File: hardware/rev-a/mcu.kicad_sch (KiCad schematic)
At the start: 46 parts, among them J10 Conn_01x05, J11 Conn_01x04, J12 Conn_01x05, J13 Conn_01x04, J14 Conn_01x04, J15 Conn_01x04, J16 Conn_01x02, Q1 NPN, SW1 SW_Push, U3 MDBT42Q-512K, U4 DS3231MZ, U5 DRV2605LDGS

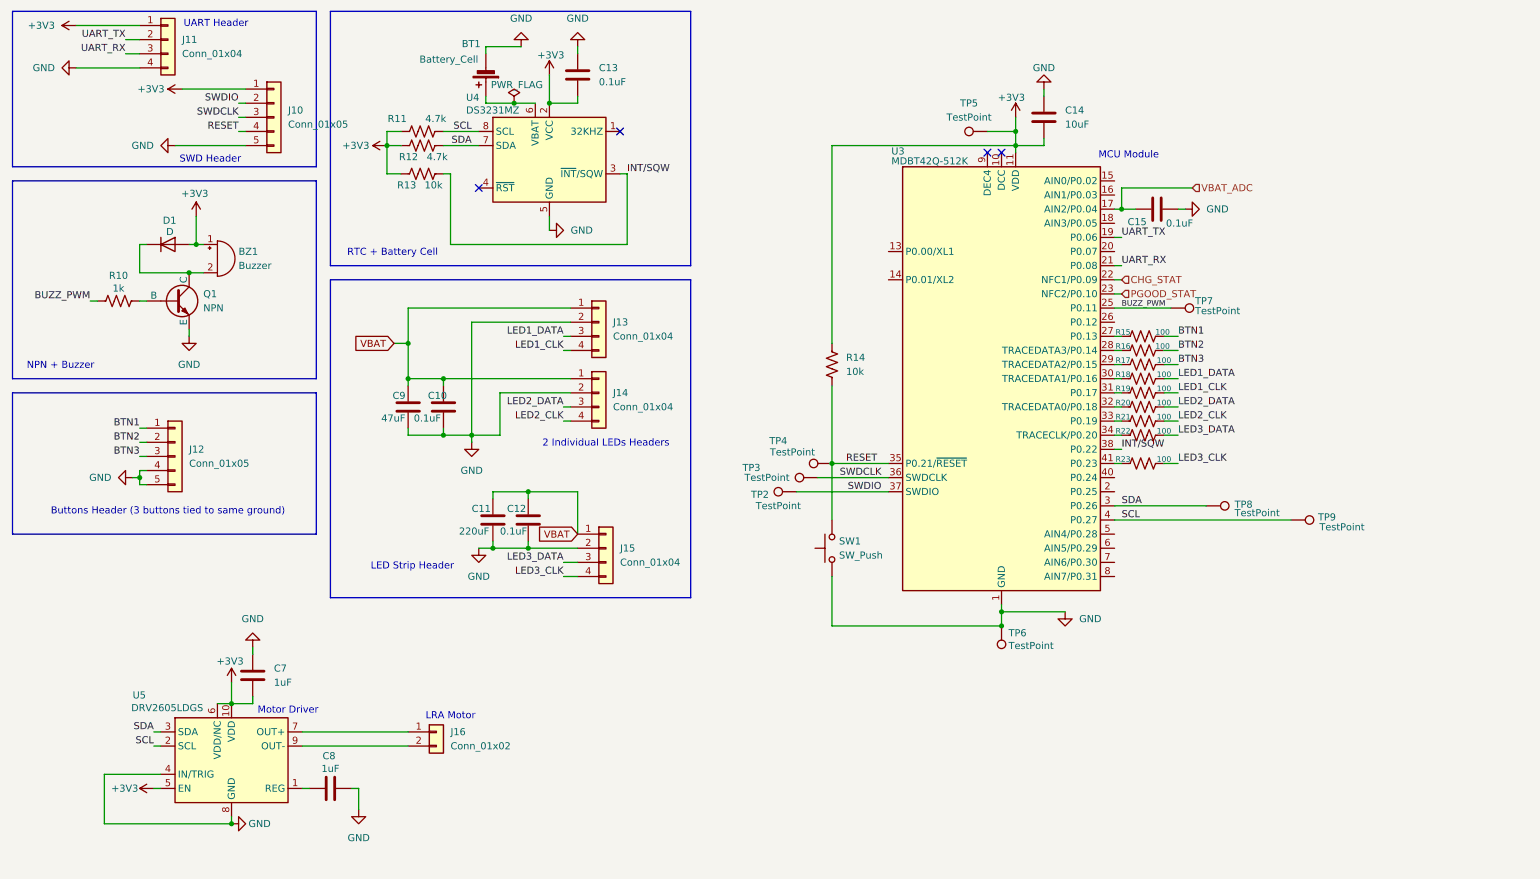
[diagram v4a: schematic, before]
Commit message: Assign footprints and add additional bypass caps
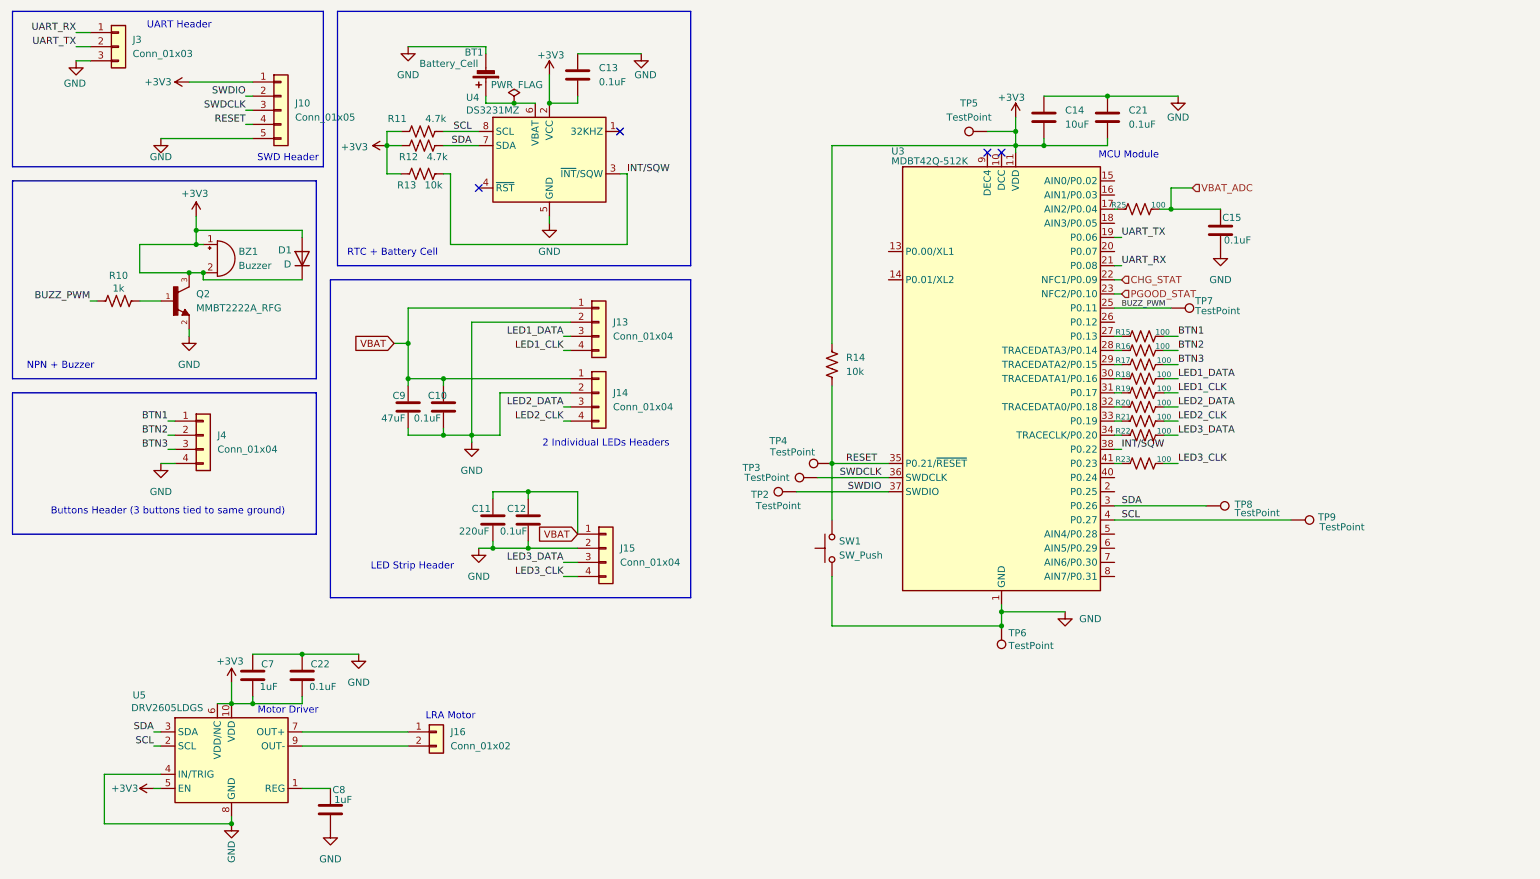
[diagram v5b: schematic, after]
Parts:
- removed J11: Conn_01x04, Connector_PinHeader_2.54mm:PinHeader_1x04_P2.54mm_Vertical, symbol Connector_Generic:Conn_01x04
- removed J12: Conn_01x05, Connector_JST:JST_PH_B5B-PH-K_1x05_P2.00mm_Vertical, symbol Connector_Generic:Conn_01x05
- removed Q1: NPN, Package_TO_SOT_SMD:SOT-23, symbol Simulation_SPICE:NPN
- added C21, C22: 0.1uF, Capacitor_SMD:C_0603_1608Metric, symbol Device:C
- added J3: Conn_01x03, Connector_PinHeader_2.54mm:PinHeader_1x03_P2.54mm_Vertical, symbol Connector_Generic:Conn_01x03
- added J4: Conn_01x04, Connector_PinHeader_2.54mm:PinHeader_1x04_P2.54mm_Vertical, symbol Connector_Generic:Conn_01x04
- added Q2: MMBT2222A_RFG, Package_TO_SOT_SMD:SOT-23, symbol MMBT2222A_RFG:MMBT2222A_RFG
- added R25: 100, Resistor_SMD:R_0603_1608Metric, symbol Device:R_US
- BT1: footprint Battery:BatteryHolder_Keystone_103_1x20mm -> Battery:BatteryHolder_Keystone_3034_1x20mm
- BZ1: footprint TerminalBlock:TerminalBlock_MaiXu_MX126-5.0-02P_1x02_P5.00mm -> CMT-1203-SMT:CUI_CMT-1203-SMT
- SW1: footprint Button_Switch_SMD:SW_SPST_TL3342 -> Button_Switch_SMD:SW_SPST_EVQP0
- U5: footprint Package_SO:VSSOP-10_3x3mm_P0.5mm -> DRV2605LDGST:SOP50P490X110-10N
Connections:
- net +3V3: now also BZ1.2 (-), D1.1 (K), C21.2, C22.2, Q2.3
- net BTN1: now also J4.1 (Pin_1)
- net BTN2: now also J4.2 (Pin_2)
- net BTN3: now also J4.3 (Pin_3)
- net GND: now also C15.1, C21.1, C22.1, J3.3 (Pin_3), J4.4 (Pin_4), Q2.2; no longer C15.2
- net UART_RX: now also J3.1 (Pin_1)
- net UART_TX: now also J3.2 (Pin_2)
- net VBAT_ADC: now also C15.2, R25.2; no longer C15.1, U3.17 (AIN2/P0.04)
- net at R10.2: now also Q2.1
- new net: R25.1, U3.17 (AIN2/P0.04)
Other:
- moved on the sheet: C15, C8, D1, J10

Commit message: format schematic to fit convention, replace SWD header with 2x5
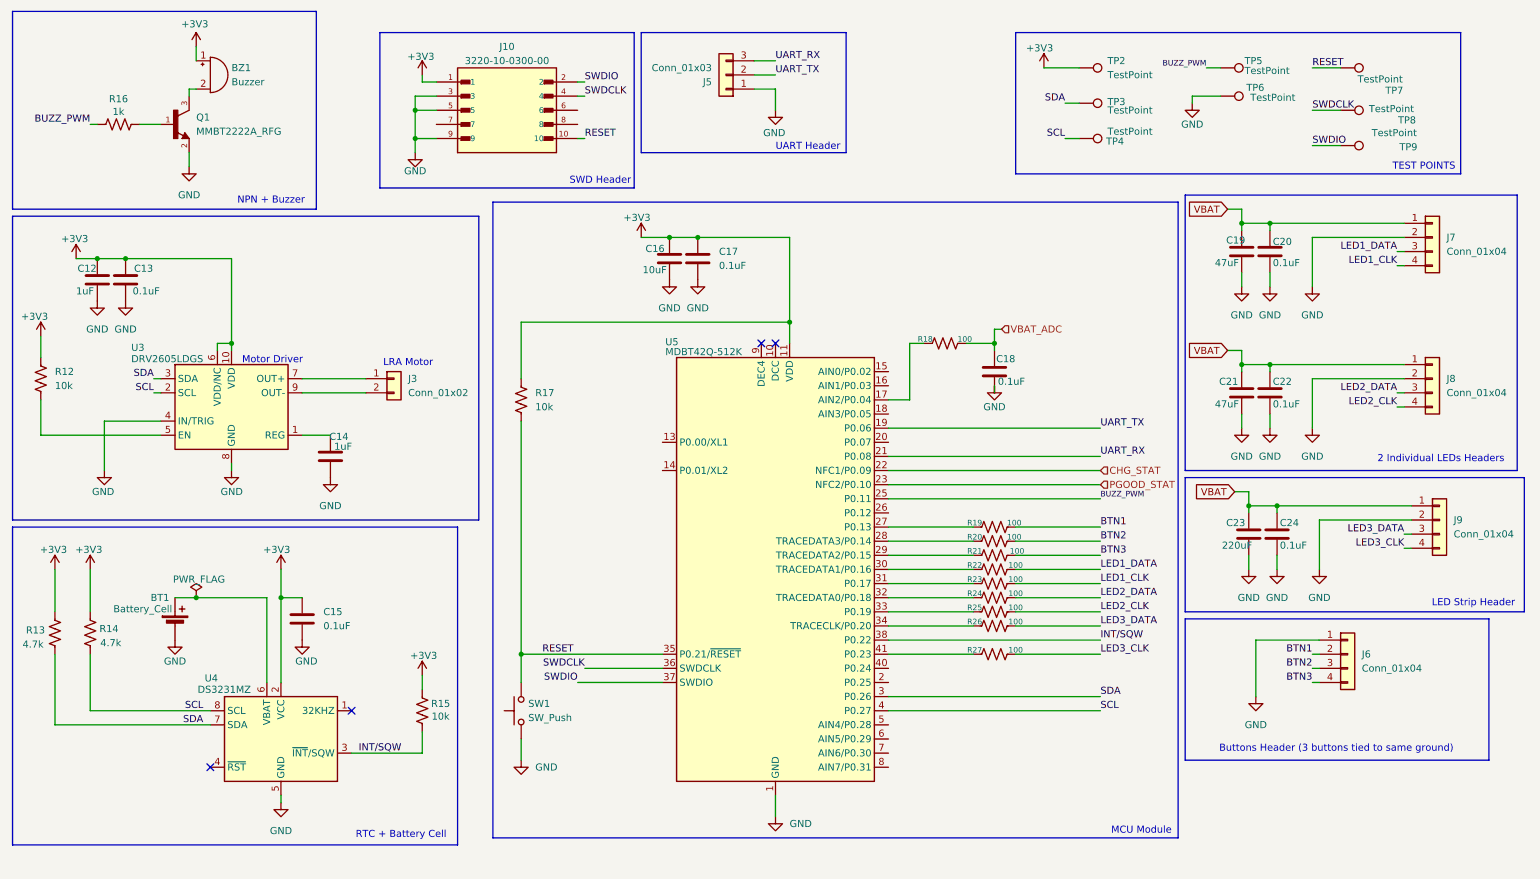
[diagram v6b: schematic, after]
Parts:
- removed C11: 220uF, Capacitor_SMD:CP_Elec_5x5.4, symbol Device:C
- removed C12: 0.1uF, Capacitor_SMD:C_0603_1608Metric, symbol Device:C
- removed D1: D, Diode_SMD:D_SOD-123, symbol Device:D
- removed J10: Conn_01x05, Connector_PinHeader_2.54mm:PinHeader_1x05_P2.54mm_Vertical, symbol Connector_Generic:Conn_01x05
- removed J14, J15: Conn_01x04, Connector_JST:JST_PH_B4B-PH-K_1x04_P2.00mm_Vertical, symbol Connector_Generic:Conn_01x04
- added C21: 47uF, Capacitor_SMD:C_0603_1608Metric, symbol Device:C
- added C22, C24: 0.1uF, Capacitor_SMD:C_0603_1608Metric, symbol Device:C
- added C23: 220uF, Capacitor_SMD:C_0603_1608Metric, symbol Device:C
- added J10: 3220-10-0300-00, Connector_PinHeader_1.27mm:PinHeader_2x05_P1.27mm_Vertical, symbol 3220-10-0300-00:3220-10-0300-00
- added J8, J9: Conn_01x04, Connector_JST:JST_PH_B4B-PH-K_1x04_P2.00mm_Vertical, symbol Connector_Generic:Conn_01x04
- added R12: 10k, Resistor_SMD:R_0603_1608Metric, symbol Device:R_US
- renumbered C7 to C12, C22 to C13, C8 to C14, C13 to C15, C14 to C16, C21 to C17, C15 to C18, C9 to C19, C10 to C20, J16 to J3, J3 to J5, J4 to J6, J13 to J7, Q2 to Q1, R12 to R13, R11 to R14, R13 to R15, R10 to R16, R14 to R17, R25 to R18, R15 to R19, R16 to R20, R17 to R21, R18 to R22, R19 to R23, R20 to R24, R21 to R25, R22 to R26, R23 to R27, TP5 to TP2, TP8 to TP3, TP9 to TP4, TP7 to TP5, TP4 to TP7, TP3 to TP8, TP2 to TP9, U5 to U3, U3 to U5
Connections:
- net +3V3: now also C12.1, C13.1, C15.1, C16.1, C17.1, R13.2, R14.2, R15.2, J10.1, R12.1; no longer BZ1.2 (-), C12.2, C13.2, C15.2, C16.2, C17.2, Q1.3, R13.1, R14.1, R15.1, U3.5 (EN)
- net BTN1: now also J6.2 (Pin_2); no longer J6.1 (Pin_1)
- net BTN2: now also J6.3 (Pin_3); no longer J6.2 (Pin_2)
- net BTN3: now also J6.4 (Pin_4); no longer J6.3 (Pin_3)
- net GND: now also C12.2, C13.2, C15.2, C16.2, C17.2, J5.1 (Pin_1), J6.1 (Pin_1), C21.2, C22.2, C23.2, C24.2, J10.3, J10.5, J10.9, J8.2 (Pin_2), J9.2 (Pin_2); no longer C12.1, C13.1, C15.1, C16.1, C17.1, J5.3 (Pin_3), J6.4 (Pin_4)
- net INT/SQW: now also R15.1; no longer R15.2
- net LED2_CLK: now also J8.4 (Pin_4)
- net LED2_DATA: now also J8.3 (Pin_3)
- net LED3_CLK: now also J9.4 (Pin_4)
- net LED3_DATA: now also J9.3 (Pin_3)
- net RESET: now also J10.10
- net SCL: now also R14.1; no longer R14.2
- net SDA: now also R13.1; no longer R13.2
- net SWDCLK: now also J10.4
- net SWDIO: now also J10.2
- net UART_RX: now also J5.3 (Pin_3); no longer J5.1 (Pin_1)
- net VBAT: now also C21.1, C22.1, C23.1, C24.1, J8.1 (Pin_1), J9.1 (Pin_1)
- new net: BZ1.2 (-), Q1.3
- new net: R12.2, U3.5 (EN)
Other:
- note added: "TEST POINTS"
- moved on the sheet: BT1, BZ1, C12, C13, C14, C15, C16, C17, C18, C19, C20, J3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

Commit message: rev c with labeled ICs
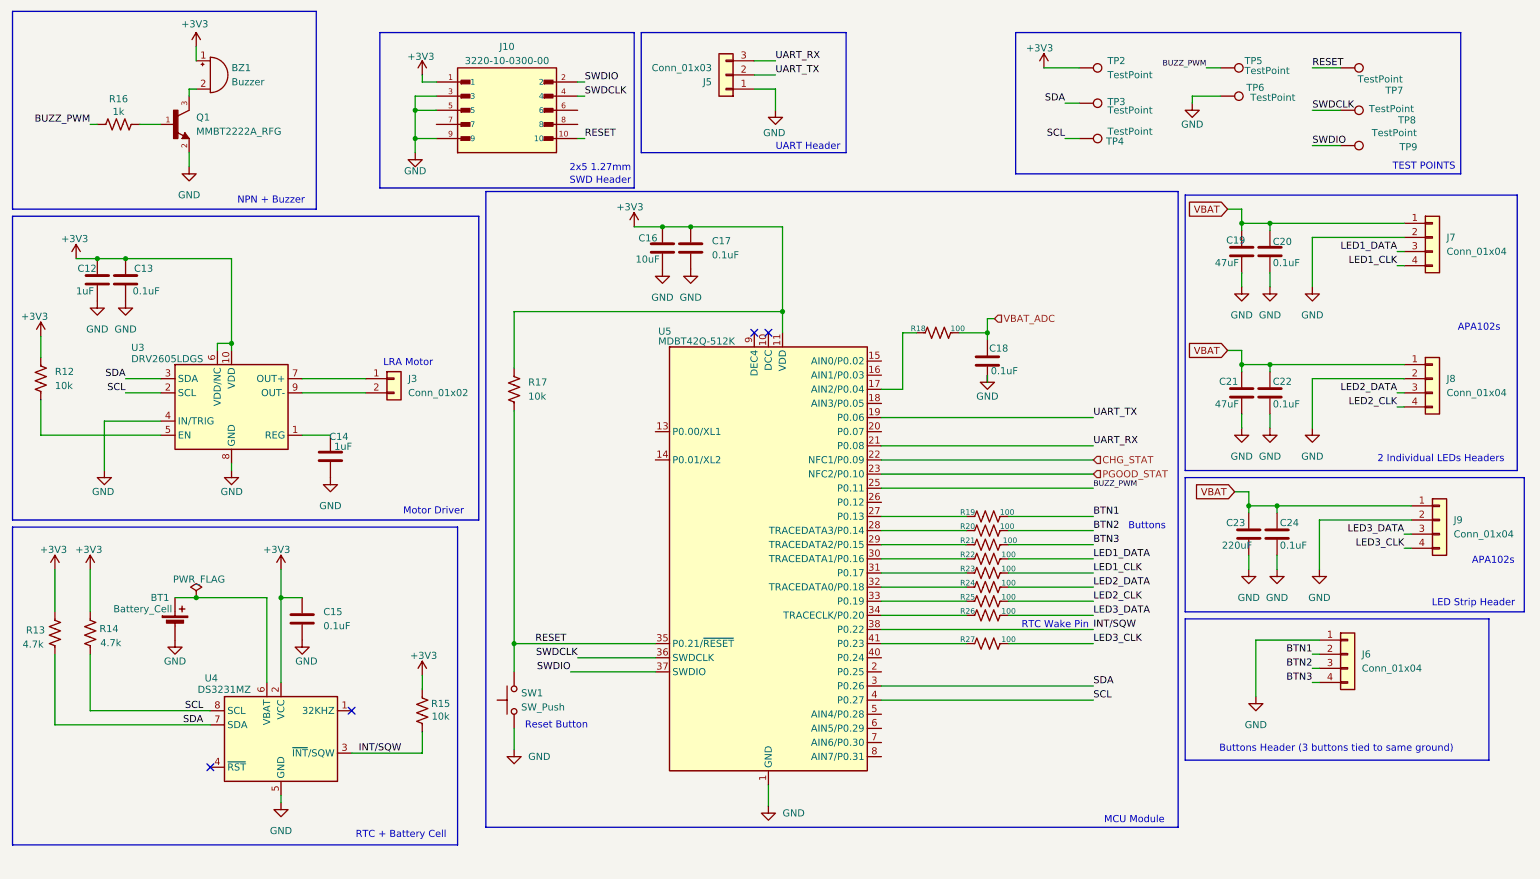
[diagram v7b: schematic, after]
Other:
- note added: "2x5 1.27mm"
- note added: "APA102s"
- note added: "Buttons"
- note added: "RTC Wake Pin"
- note added: "Reset Button"
- moved on the sheet: C16, C17, C18, R17, R18, R19, R20, R21, R22, R23, R24, R25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

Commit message: crackhead layout file added
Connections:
- net +3V3: no longer C12.1, C13.1, U3.10 (VDD), U3.6 (VDD/NC)
- net BTN1: now also R27.1; no longer R19.2
- net BTN2: now also R26.1; no longer R20.2
- net BTN3: now also R25.1; no longer R21.2
- net LED1_CLK: now also R24.1; no longer R23.1
- net LED1_DATA: now also R23.1; no longer R22.1
- net LED2_CLK: now also R22.1; no longer R25.1
- net LED2_DATA: now also R21.2; no longer R24.1
- net LED3_CLK: now also R20.2; no longer R27.1
- net LED3_DATA: now also R19.2; no longer R26.1
- net SCL: now also U5.3 (P0.26); no longer U5.4 (P0.27)
- net SDA: now also U5.2 (P0.25); no longer U5.3 (P0.26)
- net VBAT: now also C12.1, C13.1, U3.10 (VDD), U3.6 (VDD/NC)
- net at R21.1: now also U5.28 (TRACEDATA3/P0.14); no longer U5.29 (TRACEDATA2/P0.15)
- net at U5.26 (P0.12): now also R19.1
- net at U5.27 (P0.13): now also R20.1; no longer R19.1
- net at R22.2: now also U5.29 (TRACEDATA2/P0.15); no longer U5.30 (TRACEDATA1/P0.16)
- net at R23.2: now also U5.30 (TRACEDATA1/P0.16); no longer U5.31 (P0.17)
- net at R24.2: now also U5.31 (P0.17); no longer U5.32 (TRACEDATA0/P0.18)
- net at R25.2: now also U5.32 (TRACEDATA0/P0.18); no longer U5.33 (P0.19)
- net at R26.2: now also U5.33 (P0.19); no longer U5.34 (TRACECLK/P0.20)
- net at R27.2: now also U5.34 (TRACECLK/P0.20); no longer U5.41 (P0.23)
- no-connect marks 4 -> 11
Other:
- moved on the sheet: C16, C17, C18, R17, R18, R19, R20, R21, R22, R23, R24, R25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
